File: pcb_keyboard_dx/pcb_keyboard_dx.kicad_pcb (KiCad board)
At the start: 2 copper layers, 156.8 x 135.8 mm, 131 parts, among them SW1 BOOT button, U1 Pico, U2 74LVC1G34, U3 TRRS

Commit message: upload files
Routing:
- net Col 6: track 110.7 -> 108.4 mm, vias 4 -> 3

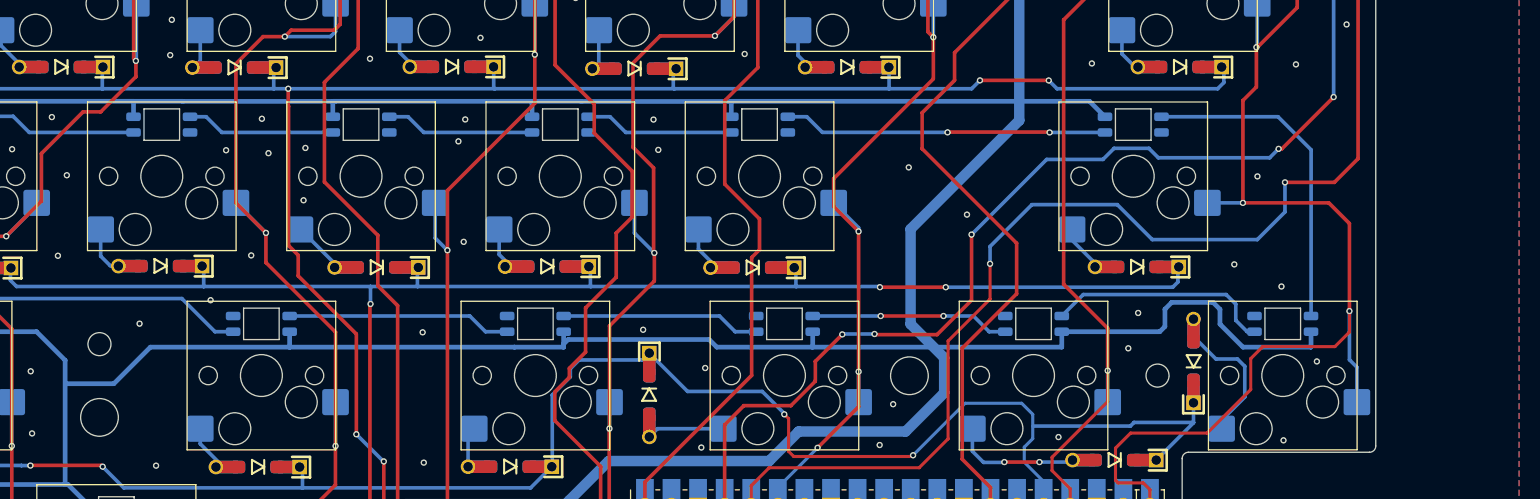
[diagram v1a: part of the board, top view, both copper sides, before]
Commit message: added d+ and d- bus
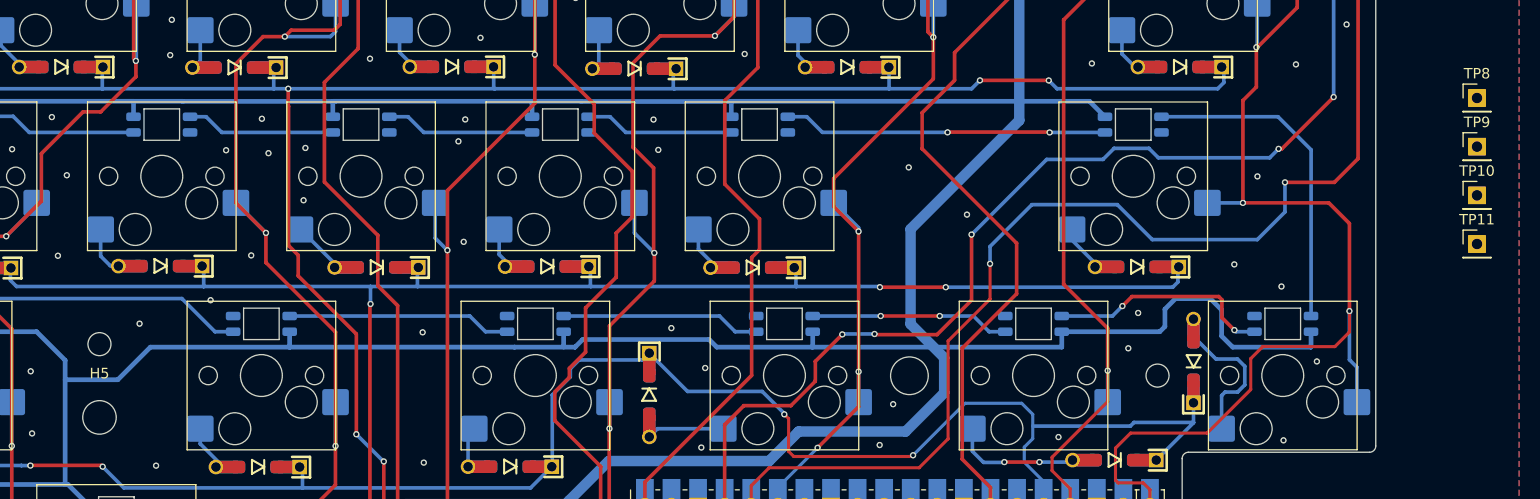
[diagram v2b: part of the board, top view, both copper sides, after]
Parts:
- added H5: MountingHole, MountingHole:MountingHole_3.2mm_M3, F.Cu at (64.3, 125.8)
- added TP10: TestPoint, Connector_PinHeader_2.54mm:PinHeader_1x01_P2.54mm_Vertical, F.Cu at (195.9, 104.6)
- added TP11: TestPoint, Connector_PinHeader_2.54mm:PinHeader_1x01_P2.54mm_Vertical, F.Cu at (195.9, 109.3)
- added TP8: TestPoint, Connector_PinHeader_2.54mm:PinHeader_1x01_P2.54mm_Vertical, F.Cu at (195.9, 95.3)
- added TP9: TestPoint, Connector_PinHeader_2.54mm:PinHeader_1x01_P2.54mm_Vertical, F.Cu at (195.9, 100.0)
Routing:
- net Net-(D36-A): track 12.7 -> 13.4 mm
- net +5V: track 1034.7 -> 1035.4 mm
- net Net-(LED31-DOUT): vias 0 -> 2
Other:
- outline, holes or cut-outs redrawn
- board text removed: "Level shifter for led"

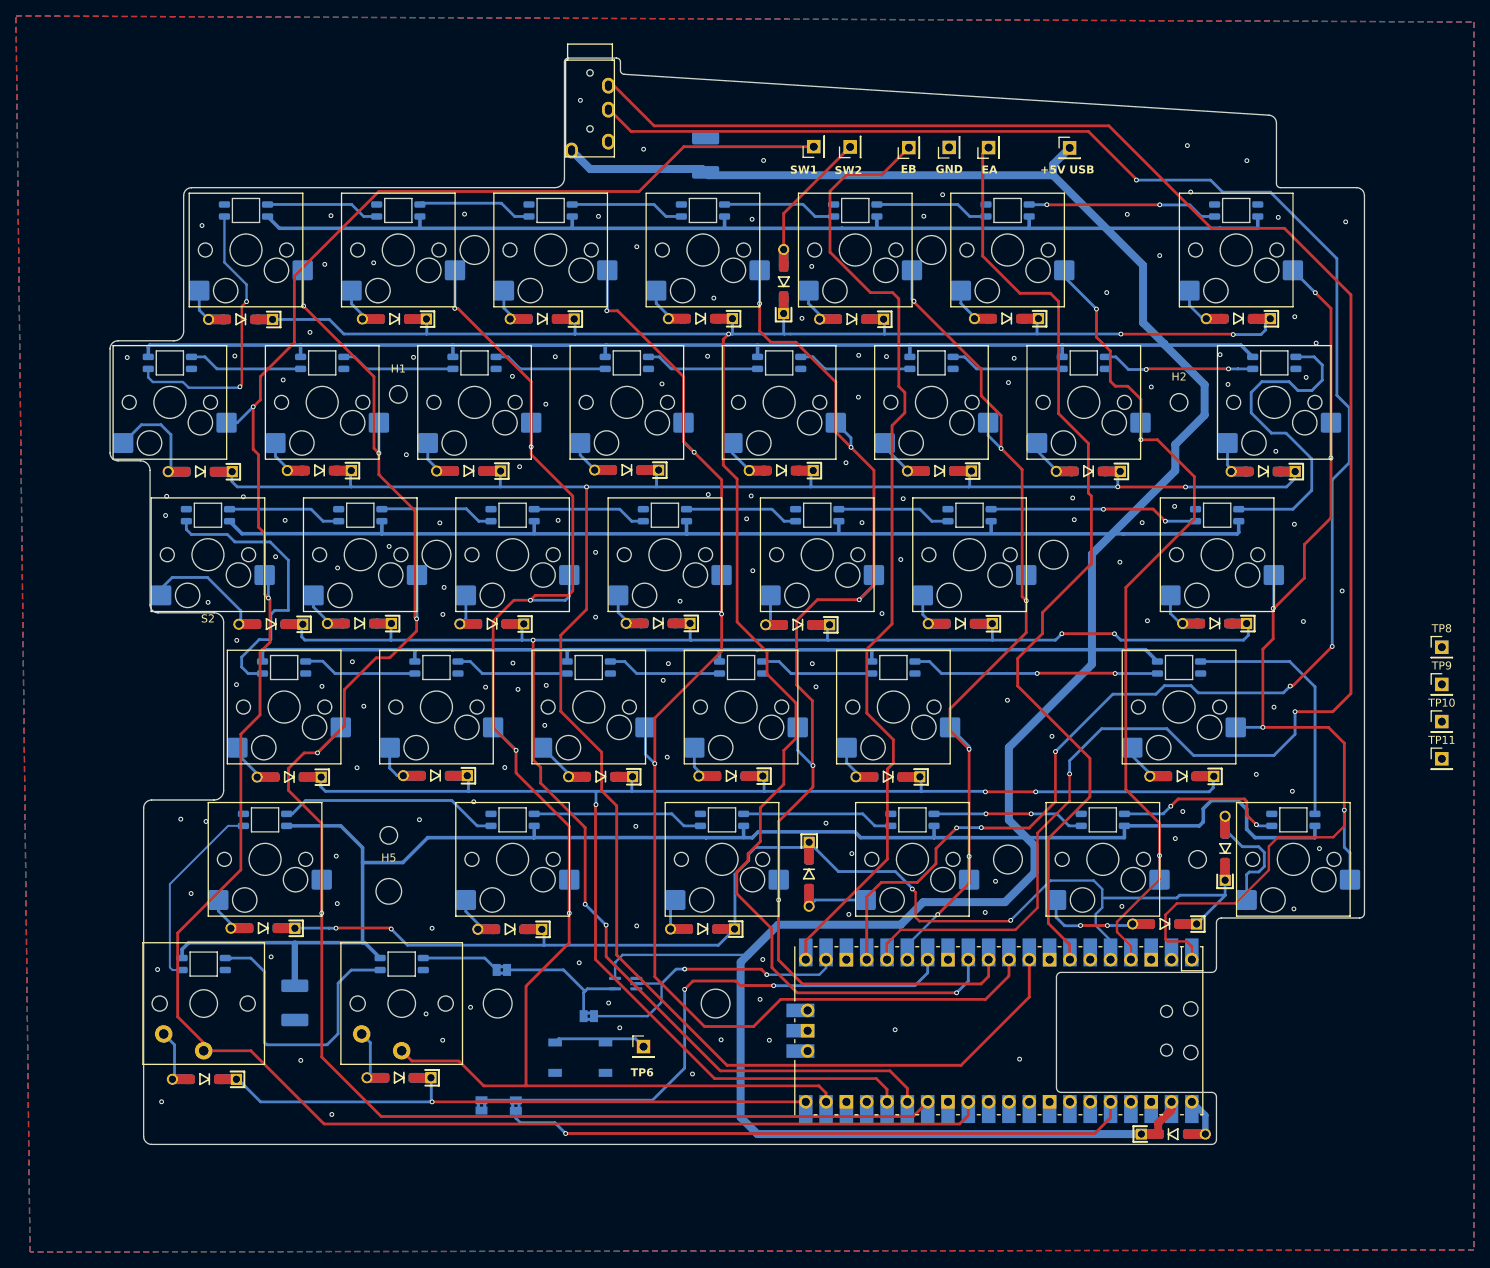
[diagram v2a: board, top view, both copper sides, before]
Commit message: stessi GPIO per dx e sx
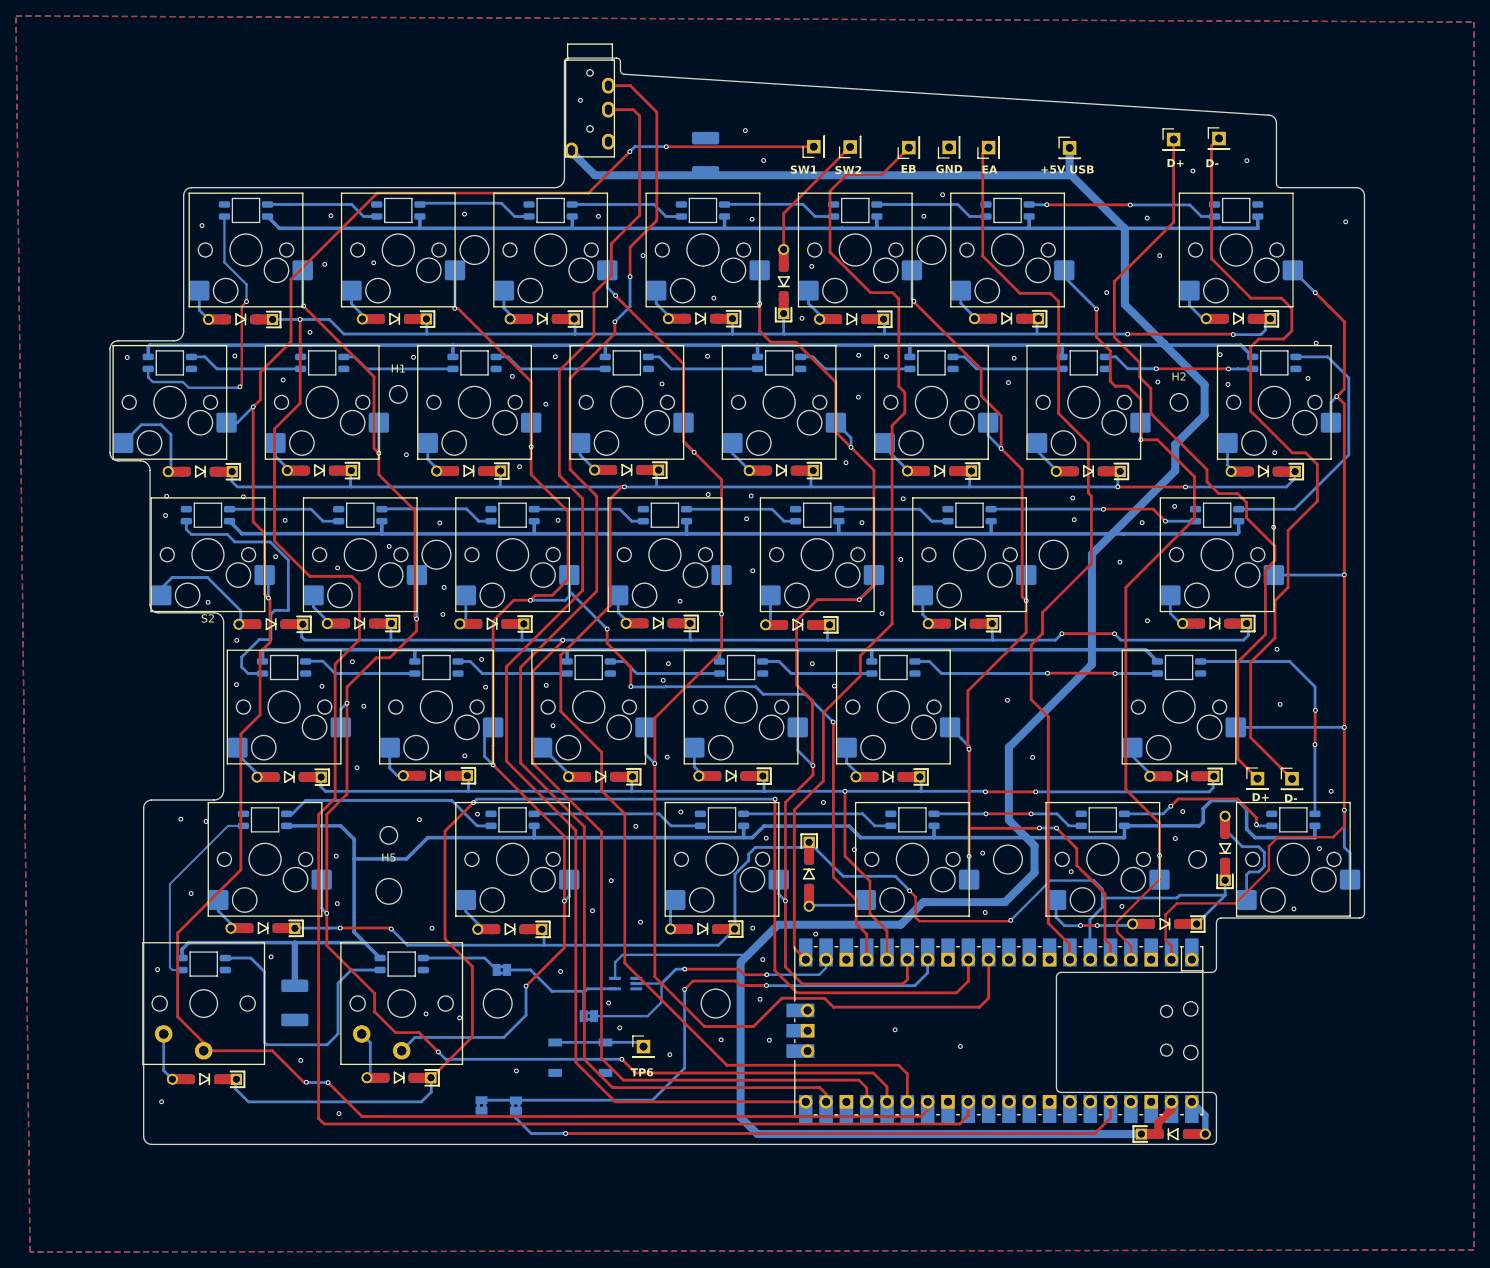
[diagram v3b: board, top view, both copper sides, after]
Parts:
- moved TP10 78.0 mm to (168.1, 31.7)
- moved TP8 71.8 mm to (162.4, 31.8)
- moved TP9 25.9 mm to (172.9, 111.7)
- moved TP11 18.9 mm to (177.2, 111.8)
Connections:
- U1 pad 1: Col 7 -> unconnected-(U1-GPIO0-Pad1)
- U1 pad 10: Col 3 -> unconnected-(U1-GPIO7-Pad10)
- U1 pad 11: Col 4 -> Col 3
- U1 pad 12: Row 0 -> Row 5
- U1 pad 15: Col 5 -> Col 4
- U1 pad 16: TX -> Row 3
- U1 pad 17: RX -> Col 2
- U1 pad 2: unconnected-(U1-GPIO1-Pad2) -> Col 7
- U1 pad 21: Row 5 -> RX
- U1 pad 22: Col 2 -> TX
- U1 pad 24: unconnected-(U1-GPIO18-Pad24) -> Row 2
- U1 pad 25: Row 3 -> Col 1
- U1 pad 26: Row 2 -> Row 1
- U1 pad 27: Col 1 -> Col 0
- U1 pad 29: Col 0 -> Row 0
- U1 pad 5: Row 4 -> Col 5
- U1 pad 6: unconnected-(U1-GPIO4-Pad6)_1 -> Row 4
- U1 pad 9: Row 1 -> unconnected-(U1-GPIO6-Pad9)
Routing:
- net Data-: track 0.00 -> 100.8 mm
- net Data+: track 0.00 -> 95.6 mm
- net Row 5: track 75.8 -> 156.6 mm, vias 1 -> 2
- net Row 0: track 256.4 -> 333.6 mm, vias 4 -> 3
- net TX: track 239.3 -> 171.9 mm
- net RX: track 233.9 -> 166.8 mm, vias 6 -> 0
- net Row 3: track 188.4 -> 145.8 mm
- net Col 2: track 197.6 -> 223.5 mm, vias 5 -> 9
- net Col 1: track 212.0 -> 193.7 mm, vias 5 -> 7
- net Row 1: track 276.2 -> 258.8 mm
- net Col 5: track 113.9 -> 126.2 mm, vias 6 -> 7
- net Col 4: track 149.5 -> 139.3 mm
- net Net-(LED33-DIN): track 42.6 -> 33.9 mm
- net Col 0: track 286.3 -> 280.1 mm, vias 2 -> 6
- net encoder A: track 120.5 -> 114.8 mm
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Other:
- board text added: "D+"
- board text added: "D-"
